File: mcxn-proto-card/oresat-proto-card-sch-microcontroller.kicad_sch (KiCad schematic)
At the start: 103 parts, among them J9 SM14B-SHLS-TF, U1 MCXN947VKLT, U8 TCAN330, Y2 24 MHz

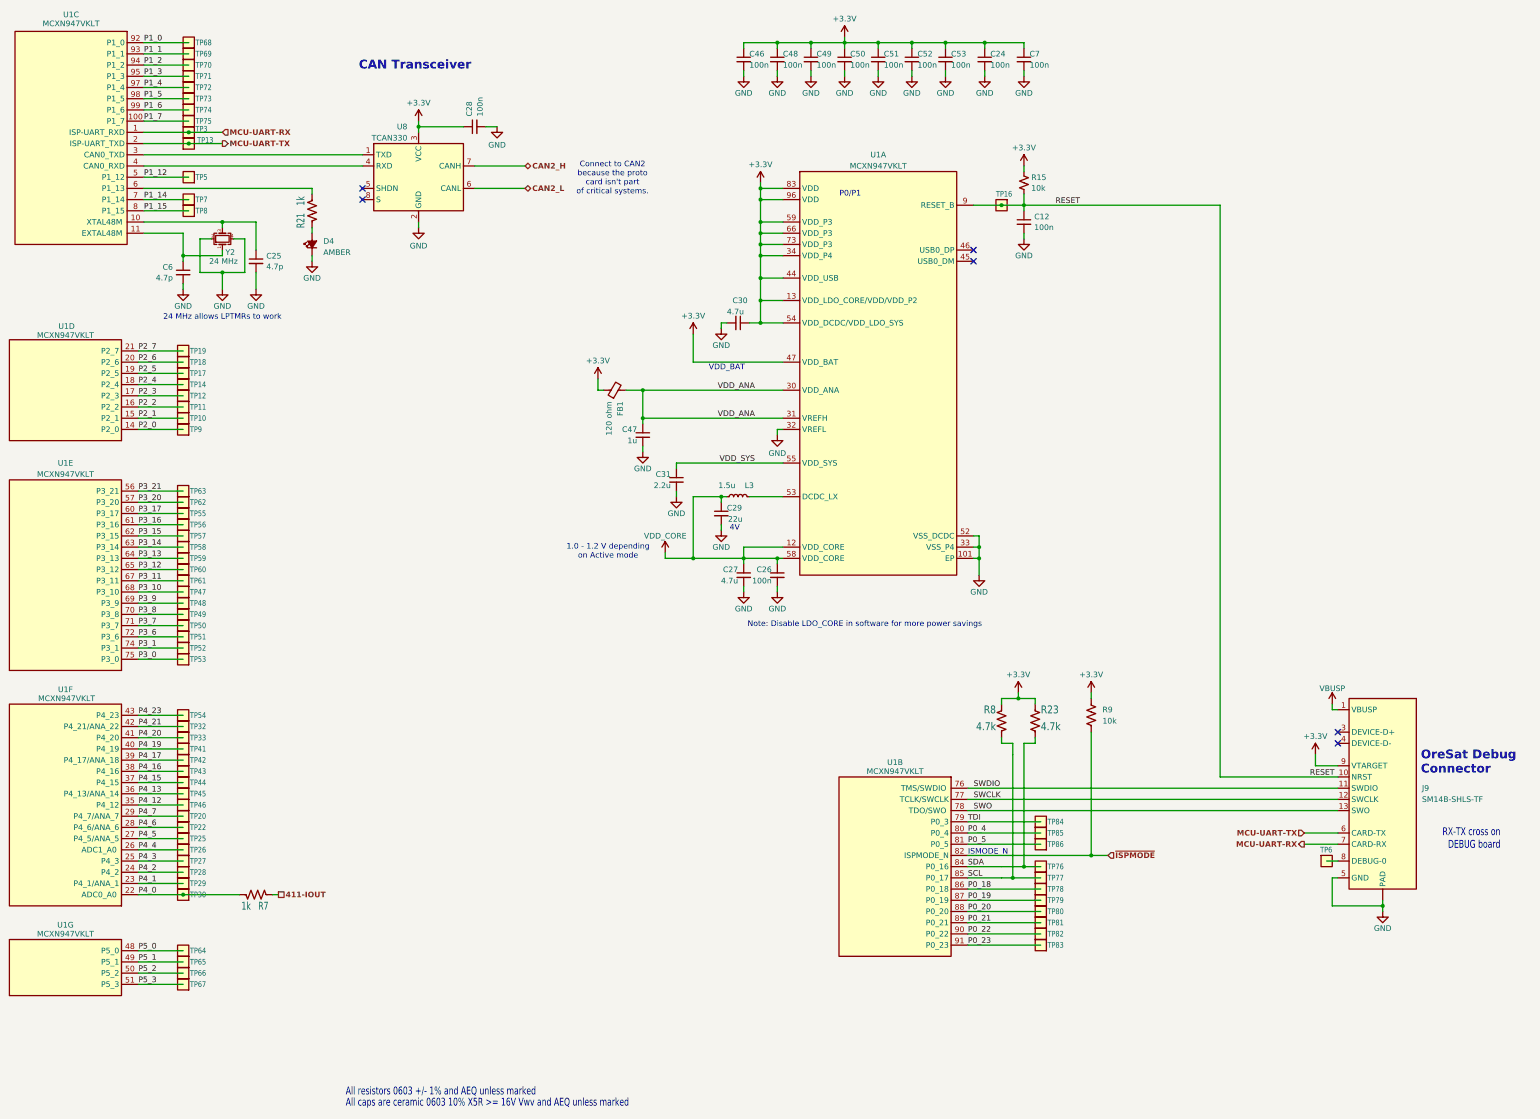
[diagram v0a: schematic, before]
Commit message: Update protocard
Update to 10.0.4, new .gitignore, better hierachical layout, updated footprints, re-arranged LEDs, brought outline and SMPMs into latest standards, all but OPD is updated.
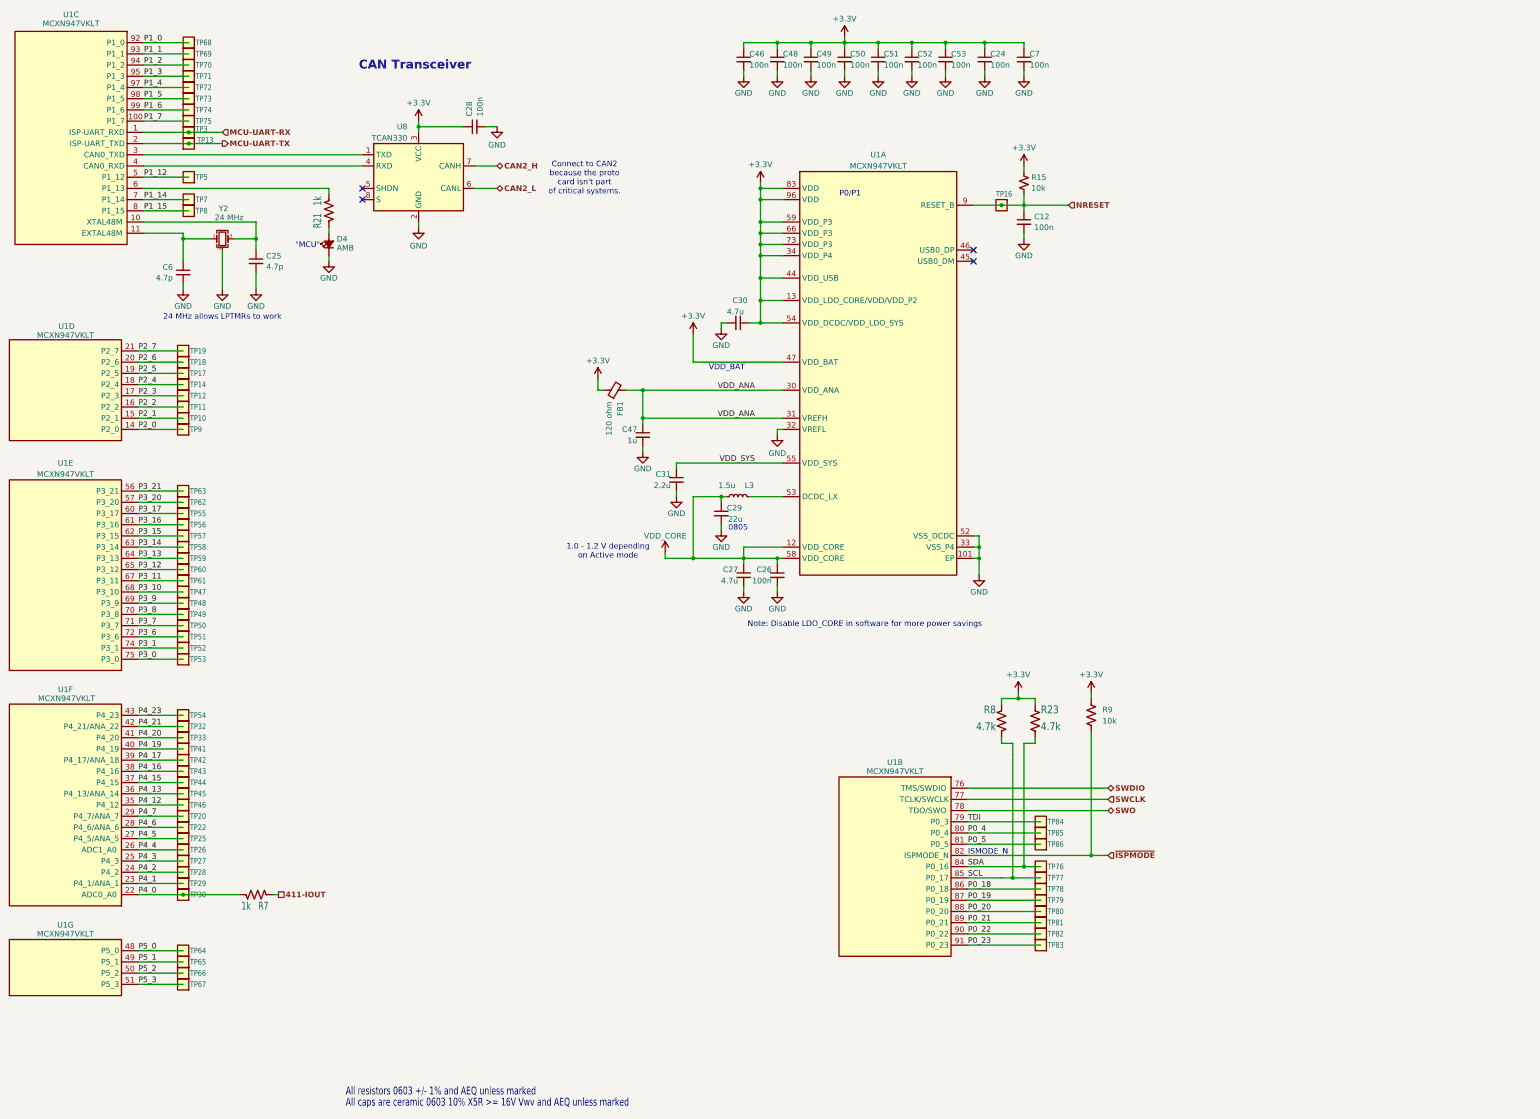
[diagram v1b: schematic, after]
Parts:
- removed J9: SM14B-SHLS-TF, oresat-connectors:J-JST-SM14BSHLSTF, symbol oresat-connectors:ORESAT-DEBUG-CONNECTOR-3
- removed TP6: Test-Point, oresat-misc:TestPoint-0.75mm-th, symbol oresat-misc:Test-Point-0.75mm-th
- C29: footprint oresat-passives:0603-C-NOSILK -> oresat-passives:0805-C-NOSILK; DPN 478-KAM15CT70G226KTCT-ND -> 490-GRT21BC81C226ME13LCT-ND; MFR KYOCERA AVX -> Murata Electronics; MPN KAM15CT70G226KT -> GRT21BC81C226ME13L
- D4: value AMBER -> AMB
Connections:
- net RESET renamed NRESET
- no-connect marks 6 -> 4
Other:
- note added: ""MCU""
- note added: "0805"
- note removed: "4V"
- note removed: "OreSat Debug Connector"
- note removed: "RX-TX cross on DEBUG board"
- moved on the sheet: D4, R21

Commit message: Small cleanups for manufacturing
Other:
- moved on the sheet: R23, R8, R9, TP76, TP77, TP78, TP79, TP80, TP81, TP82, TP83, TP84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
